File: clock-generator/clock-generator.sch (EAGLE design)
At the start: 106 parts, among them IC1 TLV9001, IC2 24C00TS, K1 694108106102, M1 MENTOR_12701001, T1 BC847, U1 SN74LVC1G04DBV, U2 SI5351C, U3 IP4234CZ6, U4 ATSAMD21E, U5 ADP151AUJZ, U6 IP4234CZ6, X1 MINI-USB-SHIELD-UX60A-MB-5ST, X4 JACK2.5_SJ-2523, X5 UEXT/90

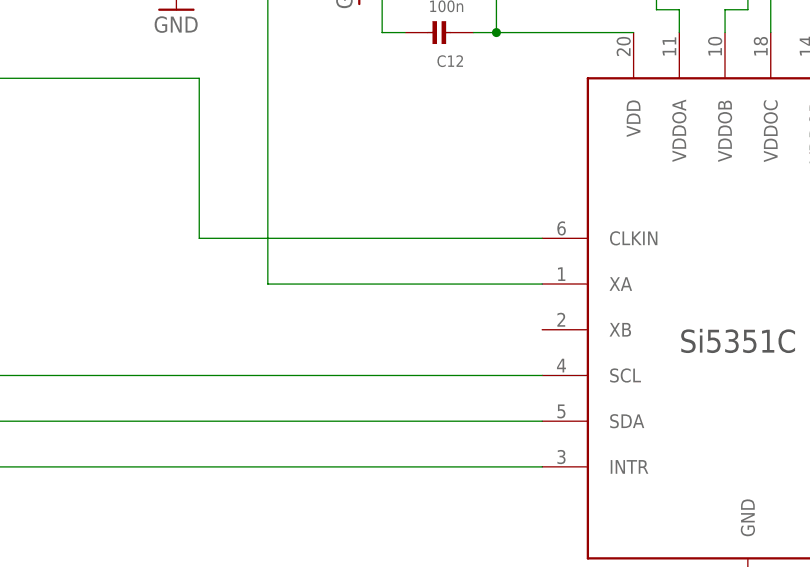
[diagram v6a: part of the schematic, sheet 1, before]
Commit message: osmo-clock-gen: capacitive coupling for XA input needed - added 100n
This was a remark by tnt, thanks.
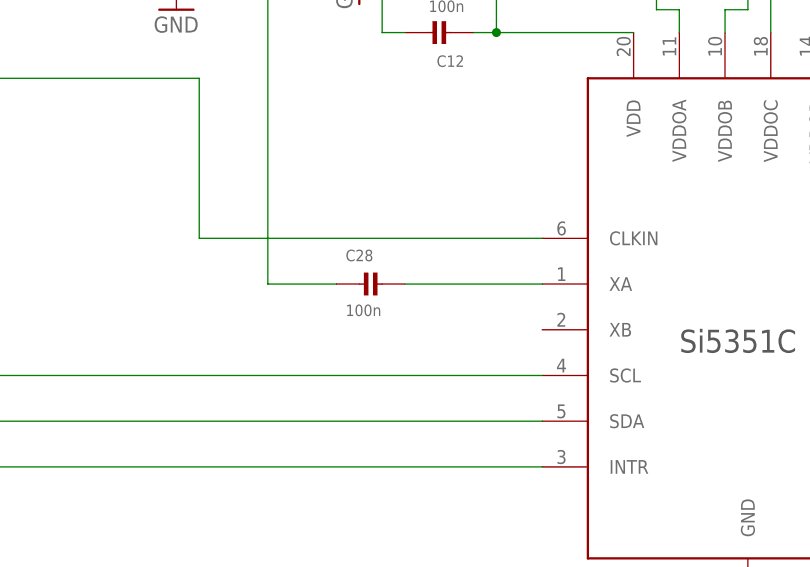
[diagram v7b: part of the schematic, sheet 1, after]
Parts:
- added C28: 100n, rc-sysmocom:CAP_CERAMIC_0603
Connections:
- new net N$8: C28.2, U2.XA
- net N$4: now also C28.1; no longer U2.XA

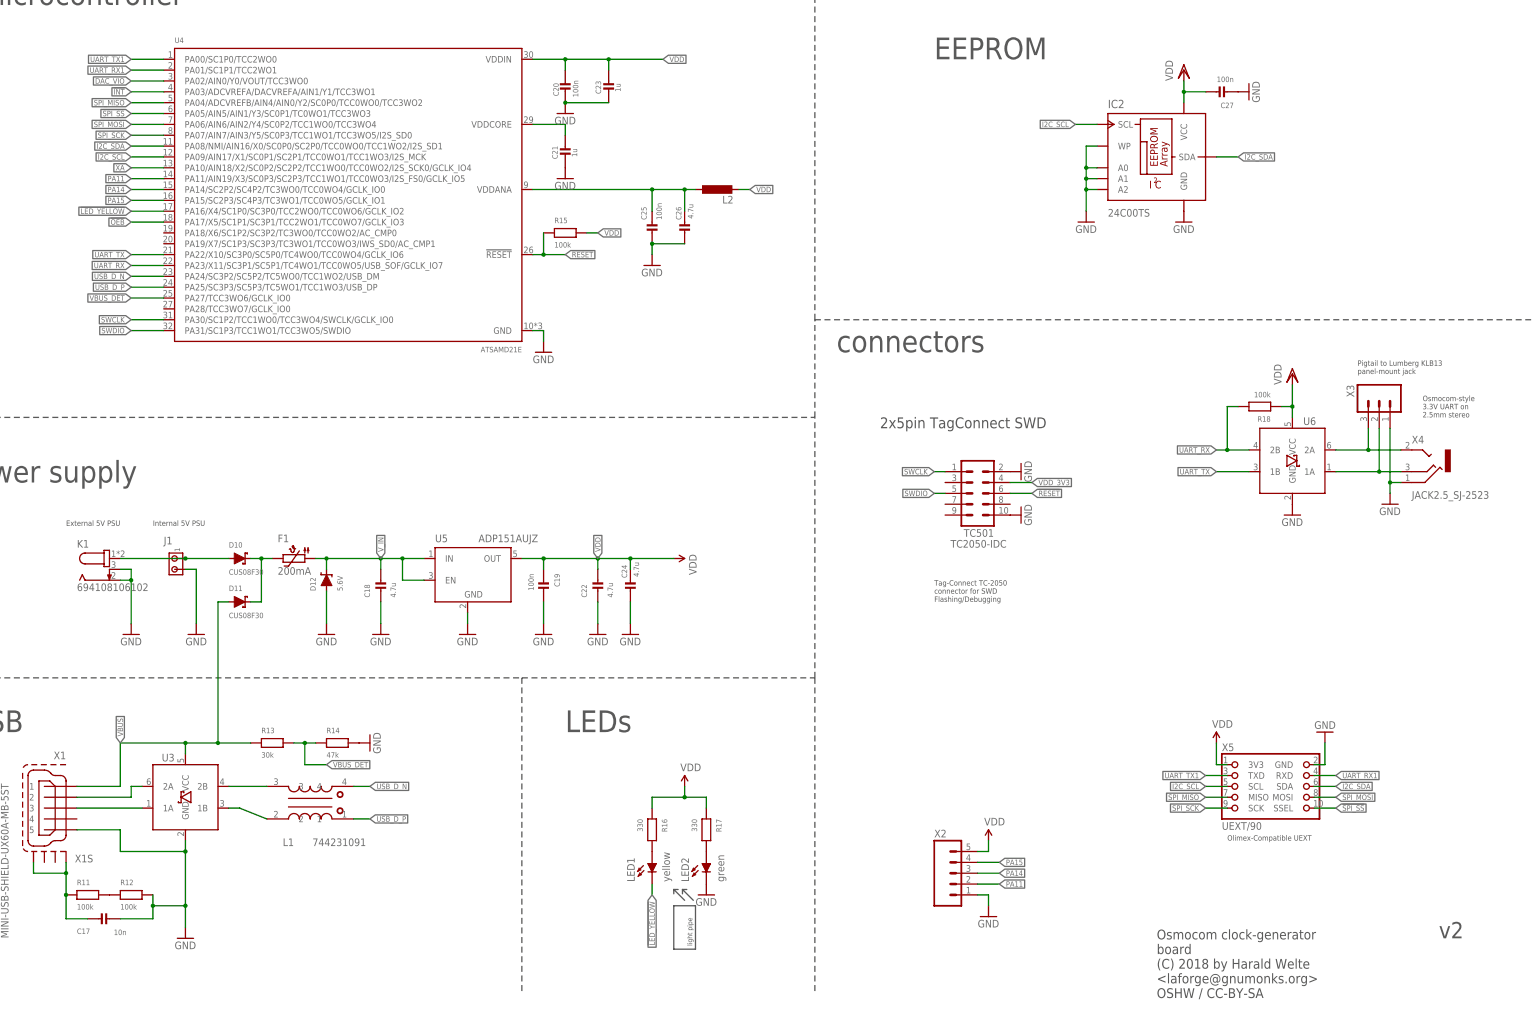
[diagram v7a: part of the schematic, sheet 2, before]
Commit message: <osmo-clock-gen: add more TVS for exposed signals, clean up and finish
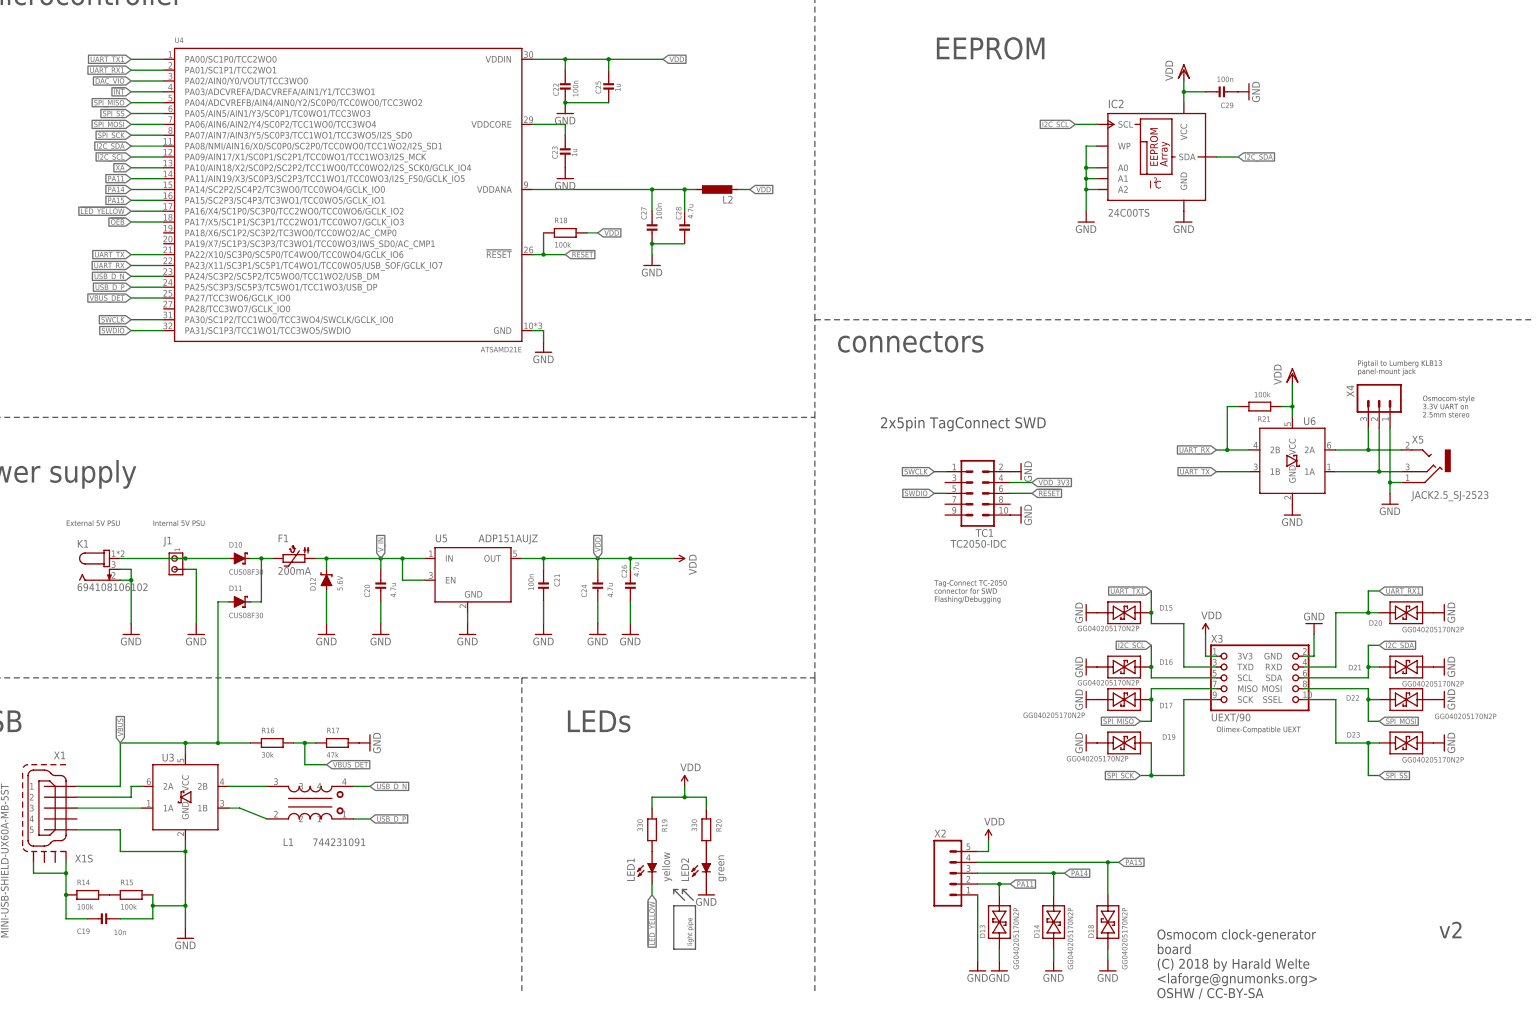
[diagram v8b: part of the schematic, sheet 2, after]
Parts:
- added C29: 100n, rc-sysmocom:CAP_CERAMIC_0603
- added D13, D14, D15, D16, D17, D18, D19, D20, D21, D22, D23: GG040205170N2P, diodes-sysmocom:TVSDIODE-BIDI-0402
- C1, C19, C2: value 100n -> 10n; device rc-sysmocom:CAP_CERAMIC_0603 -> rc-sysmocom:CAP_CERAMIC_0402; DESCRIPTION CAP CER 0.1UF 16V X7R 0603 -> CAP CER 10000PF 25V X7R 0402; LINK https://www.digikey.de/product-detail/de/samsung-electro-mechanics/CL10B104KO8NNNC/1276-1005-1-ND/3889091 -> https://www.digikey.de/product-detail/de/samsung-electro-mechanics/CL05B103KA5NNNC/1276-1057-1-ND/3889143; MANUFACTURERPARTNUMBER CL10B104KO8NNNC -> CL05B103KA5NNNC; SOURCEPARTNUMBER 1276-1005-1-ND -> 1276-1057-1-ND
- C10: value 22u -> 100n; device rc-sysmocom:CAP_CERAMIC_0805 -> rc-sysmocom:CAP_CERAMIC_0402; DESCRIPTION CAP CER 22UF 6.3V 20% X5R 0805 -> NO DESCRIPTION; LINK http://www.digikey.de/product-detail/de/CL21A226MQQNNNE/127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 -> UNKNOWN LINK; MANUFACTURER Samsung Electro-Mechanics America, Inc -> UNKNOWN MANUFACTURER; MANUFACTURERPARTNUMBER CL21A226MQQNNNE -> UNKNOWN MANUFACTURER PART NUMBER; POPULATED FALSE -> TRUE; ROHSCERTIFICATE Bleifrei / RoHS-konform -> UNKNOWN ROHS CERTIFICATE; SOURCE DIGIKEY -> UNKNOWN SOURCE; SOURCEPARTNUMBER 1276-1100-1-ND -> UNKNOWN SOURCE PART NUMBER
- C11, C21: value 1u -> 100n; DESCRIPTION CAP CER 1UF 10V X5R 0603 -> CAP CER 0.1UF 16V X7R 0603; LINK https://www.digikey.de/product-detail/de/samsung-electro-mechanics/CL10A105KP8NNNC/1276-1182-1-ND/3889268 -> https://www.digikey.de/product-detail/de/samsung-electro-mechanics/CL10B104KO8NNNC/1276-1005-1-ND/3889091; MANUFACTURERPARTNUMBER CL10A105KP8NNNC -> CL10B104KO8NNNC; SOURCEPARTNUMBER 1276-1182-1-ND -> 1276-1005-1-ND
- C12: value 100n -> 22u; device rc-sysmocom:CAP_CERAMIC_0603 -> rc-sysmocom:CAP_CERAMIC_0805; DESCRIPTION CAP CER 0.1UF 16V X7R 0603 -> CAP CER 22UF 6.3V 20% X5R 0805; LINK https://www.digikey.de/product-detail/de/samsung-electro-me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 -> http://www.digikey.de/product-detail/de/CL21A226MQQNNNE/127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; MANUFACTURER Samsung Electro-Mechanics -> Samsung Electro-Mechanics America, Inc; MANUFACTURERPARTNUMBER CL10B104KO8NNNC -> CL21A226MQQNNNE; POPULATED TRUE -> FALSE; SOURCEPARTNUMBER 1276-1005-1-ND -> 1276-1100-1-ND
- C13, C9: value 100n -> 1u; device rc-sysmocom:CAP_CERAMIC_0402 -> rc-sysmocom:CAP_CERAMIC_0603; DESCRIPTION NO DESCRIPTION -> CAP CER 1UF 10V X5R 0603; LINK UNKNOWN LINK -> https://www.digikey.de/product-detail/de/samsung-electro-me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; MANUFACTURER UNKNOWN MANUFACTURER -> Samsung Electro-Mechanics; MANUFACTURERPARTNUMBER UNKNOWN MANUFACTURER PART NUMBER -> CL10A105KP8NNNC; ROHSCERTIFICATE UNKNOWN ROHS CERTIFICATE -> Bleifrei / RoHS-konform; SOURCE UNKNOWN SOURCE -> DIGIKEY; SOURCEPARTNUMBER UNKNOWN SOURCE PART NUMBER -> 1276-1182-1-ND
- C14: device rc-sysmocom:CAP_CERAMIC_0402 -> rc-sysmocom:CAP_CERAMIC_0603; DESCRIPTION NO DESCRIPTION -> CAP CER 0.1UF 16V X7R 0603; LINK UNKNOWN LINK -> https://www.digikey.de/product-detail/de/samsung-electro-me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; MANUFACTURER UNKNOWN MANUFACTURER -> Samsung Electro-Mechanics; MANUFACTURERPARTNUMBER UNKNOWN MANUFACTURER PART NUMBER -> CL10B104KO8NNNC; ROHSCERTIFICATE UNKNOWN ROHS CERTIFICATE -> Bleifrei / RoHS-konform; SOURCE UNKNOWN SOURCE -> DIGIKEY; SOURCEPARTNUMBER UNKNOWN SOURCE PART NUMBER -> 1276-1005-1-ND
- C17: value 10n -> 100n; DESCRIPTION CAP CER 10000PF 25V X7R 0402 -> NO DESCRIPTION; LINK https://www.digikey.de/product-detail/de/samsung-electro-me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 -> UNKNOWN LINK; MANUFACTURER Samsung Electro-Mechanics -> UNKNOWN MANUFACTURER; MANUFACTURERPARTNUMBER CL05B103KA5NNNC -> UNKNOWN MANUFACTURER PART NUMBER; ROHSCERTIFICATE Bleifrei / RoHS-konform -> UNKNOWN ROHS CERTIFICATE; SOURCE DIGIKEY -> UNKNOWN SOURCE; SOURCEPARTNUMBER 1276-1057-1-ND -> UNKNOWN SOURCE PART NUMBER
- C18: value 4.7u -> 100n; device rc-sysmocom:CAP_CERAMIC_0805 -> rc-sysmocom:CAP_CERAMIC_0402; DESCRIPTION CAP CER 4.7UF 16V X5R 0805 -> NO DESCRIPTION; LINK https://www.digikey.de/product-detail/de/samsung-electro-me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 -> UNKNOWN LINK; MANUFACTURER Samsung Electro-Mechanics -> UNKNOWN MANUFACTURER; MANUFACTURERPARTNUMBER CL21A475KOFNNNE -> UNKNOWN MANUFACTURER PART NUMBER; ROHSCERTIFICATE Bleifrei / RoHS-konform -> UNKNOWN ROHS CERTIFICATE; SOURCE DIGIKEY -> UNKNOWN SOURCE; SOURCEPARTNUMBER 1276-1065-1-ND -> UNKNOWN SOURCE PART NUMBER
- C20: value 100n -> 4.7u; device rc-sysmocom:CAP_CERAMIC_0402 -> rc-sysmocom:CAP_CERAMIC_0805; DESCRIPTION CAP CER 0.1UF 10V X5R 0402 -> CAP CER 4.7UF 16V X5R 0805; LINK https://www.digikey.de/product-detail/de/samsung-electro-mechanics/CL05A104MP5NNNC/1276-1443-1-ND/3889529 -> https://www.digikey.de/product-detail/de/samsung-electro-mechanics/CL21A475KOFNNNE/1276-1065-1-ND/3889151; MANUFACTURERPARTNUMBER CL05A104MP5NNNC -> CL21A475KOFNNNE; SOURCEPARTNUMBER 1276-1443-1-ND -> 1276-1065-1-ND
- C22: value 4.7u -> 100n; device rc-sysmocom:CAP_CERAMIC_0805 -> rc-sysmocom:CAP_CERAMIC_0402; DESCRIPTION CAP CER 4.7UF 16V X5R 0805 -> CAP CER 0.1UF 10V X5R 0402; LINK https://www.digikey.de/product-detail/de/samsung-electro-mechanics/CL21A475KOFNNNE/1276-1065-1-ND/3889151 -> https://www.digikey.de/product-detail/de/samsung-electro-mechanics/CL05A104MP5NNNC/1276-1443-1-ND/3889529; MANUFACTURERPARTNUMBER CL21A475KOFNNNE -> CL05A104MP5NNNC; SOURCEPARTNUMBER 1276-1065-1-ND -> 1276-1443-1-ND
- C25: value 100n -> 1u; device rc-sysmocom:CAP_CERAMIC_0402 -> rc-sysmocom:CAP_CERAMIC_0603; DESCRIPTION CAP CER 0.1UF 10V X5R 0402 -> CAP CER 1UF 10V X5R 0603; LINK https://www.digikey.de/product-detail/de/samsung-electro-mechanics/CL05A104MP5NNNC/1276-1443-1-ND/3889529 -> https://www.digikey.de/product-detail/de/samsung-electro-mechanics/CL10A105KP8NNNC/1276-1182-1-ND/3889268; MANUFACTURERPARTNUMBER CL05A104MP5NNNC -> CL10A105KP8NNNC; SOURCEPARTNUMBER 1276-1443-1-ND -> 1276-1182-1-ND
- C27: device rc-sysmocom:CAP_CERAMIC_0603 -> rc-sysmocom:CAP_CERAMIC_0402; DESCRIPTION CAP CER 0.1UF 16V X7R 0603 -> CAP CER 0.1UF 10V X5R 0402; LINK https://www.digikey.de/product-detail/de/samsung-electro-mechanics/CL10B104KO8NNNC/1276-1005-1-ND/3889091 -> https://www.digikey.de/product-detail/de/samsung-electro-mechanics/CL05A104MP5NNNC/1276-1443-1-ND/3889529; MANUFACTURERPARTNUMBER CL10B104KO8NNNC -> CL05A104MP5NNNC; SOURCEPARTNUMBER 1276-1005-1-ND -> 1276-1443-1-ND
- C28: value 100n -> 4.7u; device rc-sysmocom:CAP_CERAMIC_0603 -> rc-sysmocom:CAP_CERAMIC_0805; DESCRIPTION CAP CER 0.1UF 16V X7R 0603 -> CAP CER 4.7UF 16V X5R 0805; LINK https://www.digikey.de/product-detail/de/samsung-electro-mechanics/CL10B104KO8NNNC/1276-1005-1-ND/3889091 -> https://www.digikey.de/product-detail/de/samsung-electro-mechanics/CL21A475KOFNNNE/1276-1065-1-ND/3889151; MANUFACTURERPARTNUMBER CL10B104KO8NNNC -> CL21A475KOFNNNE; SOURCEPARTNUMBER 1276-1005-1-ND -> 1276-1065-1-ND
- C3, C4: value 10n -> 100n; device rc-sysmocom:CAP_CERAMIC_0402 -> rc-sysmocom:CAP_CERAMIC_0603; DESCRIPTION CAP CER 10000PF 25V X7R 0402 -> CAP CER 0.1UF 16V X7R 0603; LINK https://www.digikey.de/product-detail/de/samsung-electro-mechanics/CL05B103KA5NNNC/1276-1057-1-ND/3889143 -> https://www.digikey.de/product-detail/de/samsung-electro-mechanics/CL10B104KO8NNNC/1276-1005-1-ND/3889091; MANUFACTURERPARTNUMBER CL05B103KA5NNNC -> CL10B104KO8NNNC; SOURCEPARTNUMBER 1276-1057-1-ND -> 1276-1005-1-ND
- J1: CLASS (none) -> CONNECTOR\JUMPER; DESCRIPTION (none) -> NO DESCRIPTION; LINK (none) -> UNKNOWN LINK; MANUFACTURER (none) -> UNKNOWN MANUFACTURER; MANUFACTURERPARTNUMBER (none) -> UNKNOWN MANUFACTURER PART NUMBER; POPULATED (none) -> TRUE; ROHSCERTIFICATE (none) -> UNKNOWN ROHS CERTIFICATE; SOURCE (none) -> UNKNOWN SOURCE; SOURCEPARTNUMBER (none) -> UNKNOWN SOURCE PART NUMBER
- R11: value 100k -> 0; DESCRIPTION RES SMD 100K OHM 5%% 1/10W 0603 -> RES 0.0 OHM 1/10W JUMP 0603; LINK https://www.digikey.de/product-detail/de/yageo/RC0603JR-071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 -> http://www.digikey.de/product-detail/de/foo/1276-3510-1-ND; MANUFACTURER Yageo -> Samsung Electro-Mechanics America, Inc; MANUFACTURERPARTNUMBER RC0603JR-07100KL -> RC1608J000CS; SOURCEPARTNUMBER 311-100KGRCT-ND -> 1276-3510-1-ND
- R12: value 100k -> 47k; DESCRIPTION RES SMD 100K OHM 5%% 1/10W 0603 -> RES SMD 47K OHM 5%% 1/10W 0603; LINK https://www.digikey.de/product-detail/de/yageo/RC0603JR-071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 -> https://www.digikey.de/product-detail/de/yageo/RC0603JR-074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; MANUFACTURERPARTNUMBER RC0603JR-07100KL -> RC0603JR-0747KL; SOURCEPARTNUMBER 311-100KGRCT-ND -> 311-47KGRCT-ND
- R14: value 47k -> 100k; DESCRIPTION RES SMD 47K OHM 5%% 1/10W 0603 -> RES SMD 100K OHM 5%% 1/10W 0603; LINK https://www.digikey.de/product-detail/de/yageo/RC0603JR-074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 -> https://www.digikey.de/product-detail/de/yageo/RC0603JR-071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; MANUFACTURERPARTNUMBER RC0603JR-0747KL -> RC0603JR-07100KL; SOURCEPARTNUMBER 311-47KGRCT-ND -> 311-100KGRCT-ND
- R16: value 330 -> 30k; DESCRIPTION RES 330 OHM 5%% 1/10W 0603 -> RES SMD 30K OHM 5%% 1/10W 0603; LINK https://www.digikey.de/product-detail/de/stackpole-electron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 -> https://www.digikey.de/product-detail/de/yageo/RC0603JR-073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; MANUFACTURER Stackpole Electronics Inc. -> Yageo; MANUFACTURERPARTNUMBER RMCF0603JT330R -> RC0603JR-0730KL; SOURCEPARTNUMBER RMCF0603JT330RCT-ND -> 311-30KGRCT-ND
- R17: value 330 -> 47k; DESCRIPTION RES 330 OHM 5%% 1/10W 0603 -> RES SMD 47K OHM 5%% 1/10W 0603; LINK https://www.digikey.de/product-detail/de/stackpole-electron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 -> https://www.digikey.de/product-detail/de/yageo/RC0603JR-074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; MANUFACTURER Stackpole Electronics Inc. -> Yageo; MANUFACTURERPARTNUMBER RMCF0603JT330R -> RC0603JR-0747KL; SOURCEPARTNUMBER RMCF0603JT330RCT-ND -> 311-47KGRCT-ND
- R19: value 30k -> 330; DESCRIPTION RES SMD 30K OHM 5%% 1/10W 0603 -> RES 330 OHM 5%% 1/10W 0603; LINK https://www.digikey.de/product-detail/de/yageo/RC0603JR-073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 -> https://www.digikey.de/product-detail/de/stackpole-electron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; MANUFACTURER Yageo -> Stackpole Electronics Inc.; MANUFACTURERPARTNUMBER RC0603JR-0730KL -> RMCF0603JT330R; SOURCEPARTNUMBER 311-30KGRCT-ND -> RMCF0603JT330RCT-ND
- R20: value 47k -> 330; DESCRIPTION RES SMD 47K OHM 5%% 1/10W 0603 -> RES 330 OHM 5%% 1/10W 0603; LINK https://www.digikey.de/product-detail/de/yageo/RC0603JR-074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 -> https://www.digikey.de/product-detail/de/stackpole-electron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; MANUFACTURER Yageo -> Stackpole Electronics Inc.; MANUFACTURERPARTNUMBER RC0603JR-0747KL -> RMCF0603JT330R; SOURCEPARTNUMBER 311-47KGRCT-ND -> RMCF0603JT330RCT-ND
- R21: value 0 -> 100k; DESCRIPTION RES 0.0 OHM 1/10W JUMP 0603 -> RES SMD 100K OHM 5%% 1/10W 0603; LINK http://www.digikey.de/product-detail/de/foo/1276-3510-1-ND -> https://www.digikey.de/product-detail/de/yageo/RC0603JR-071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; MANUFACTURER Samsung Electro-Mechanics America, Inc -> Yageo; MANUFACTURERPARTNUMBER RC1608J000CS -> RC0603JR-07100KL; SOURCEPARTNUMBER 1276-3510-1-ND -> 311-100KGRCT-ND
- X3: value (none) -> UEXT/90; device laforge:PINHD-1X3LOCK_NO_SILK -> laforge:UEXT/90; DESCRIPTION NO DESCRIPTION -> CONN HEADER VERT 10POS 2.54MM; LINK UNKNOWN LINK -> https://www.digikey.de/product-detail/de/on-shore-technolog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; MANUFACTURER UNKNOWN MANUFACTURER -> On Shore Technology Inc.; MANUFACTURERPARTNUMBER UNKNOWN MANUFACTURER PART NUMBER -> 302-S101; POPULATED FALSE -> TRUE; ROHSCERTIFICATE UNKNOWN ROHS CERTIFICATE -> Bleifrei / RoHS-konform; SOURCE UNKNOWN SOURCE -> DIGIKEY; SOURCEPARTNUMBER UNKNOWN SOURCE PART NUMBER -> ED1543-ND
- X4: value JACK2.5_SJ-2523 -> (none); device laforge:JACK2.5_SJ-2523 -> laforge:PINHD-1X3LOCK_NO_SILK; DESCRIPTION CONN JACK STEREO 2.5MM SMD R/A -> NO DESCRIPTION; LINK https://www.digikey.de/product-detail/de/cui-inc/SJ-2523-SM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 -> UNKNOWN LINK; MANUFACTURER CUI Inc. -> UNKNOWN MANUFACTURER; MANUFACTURERPARTNUMBER SJ-2523-SMT-TR -> UNKNOWN MANUFACTURER PART NUMBER; POPULATED TRUE -> FALSE; ROHSCERTIFICATE Bleifrei / RoHS-konform -> UNKNOWN ROHS CERTIFICATE; SOURCE DIGIKEY -> UNKNOWN SOURCE; SOURCEPARTNUMBER CP-2523SJCT-ND -> UNKNOWN SOURCE PART NUMBER
- X5: value UEXT/90 -> JACK2.5_SJ-2523; device laforge:UEXT/90 -> laforge:JACK2.5_SJ-2523; DESCRIPTION CONN HEADER VERT 10POS 2.54MM -> CONN JACK STEREO 2.5MM SMD R/A; LINK https://www.digikey.de/product-detail/de/on-shore-technolog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 -> https://www.digikey.de/product-detail/de/cui-inc/SJ-2523-SM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; MANUFACTURER On Shore Technology Inc. -> CUI Inc.; MANUFACTURERPARTNUMBER 302-S101 -> SJ-2523-SMT-TR; SOURCEPARTNUMBER ED1543-ND -> CP-2523SJCT-ND
- renumbered TC501 to TC1
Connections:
- net !RESET: now also R18.2; no longer R15.2
- net !SPI_SS: now also D23.P$2, X3.SSEL; no longer X5.SSEL
- net CLKIN: now also C4.1; no longer C2.1
- net CLKIN_AC: now also C4.2; no longer C2.2
- net GND: now also C12.1, C13.1, C18.2, C2.1, C21.2, C28.1, C29.1, C9.2, D13.P$1, D14.P$1, D15.P$2, D16.P$2, D17.P$2, D18.P$1, D19.P$1, D20.P$1, D21.P$1, D22.P$1, D23.P$1, R13.2, R15.1, R17.1, X3.GND, X4.1, X5.RING; no longer C11.1, C12.2, C13.2, C18.1, C21.1, C4.1, C9.1, R12.1, R14.1, R19.2, X3.1, X4.RING, X5.GND
- net I2C_SCL: now also D16.P$1, X3.SCL; no longer X5.SCL
- net I2C_SDA: now also D21.P$2, X3.SDA; no longer X5.SDA
- net N$1: now also C23.2; no longer C21.2
- net N$11: now also R20.1; no longer R17.1
- net N$12: now also R19.1; no longer R16.1
- net N$13: now also C27.2, C28.2; no longer C25.2, C26.2
- net N$2: now also R11.1, R12.1; no longer R20.1, R21.1
- net N$4: now also C11.1, R12.2, R13.1; no longer C28.1, R19.1, R20.2
- net N$55: now also R14.1, R15.2; no longer R11.1, R12.2
- net N$61: now also C19.1, R14.2; no longer C17.1, R11.2
- net N$8: now also C11.2; no longer C28.2
- net PA11: now also D13.P$2
- net PA14: now also D14.P$2
- net PA15: now also D18.P$2
- net SPI_MISO: now also D17.P$1, X3.MISO; no longer X5.MISO
- net SPI_MOSI: now also D22.P$2, X3.MOSI; no longer X5.MOSI
- net SPI_SCK: now also D19.P$2, X3.SCK; no longer X5.SCK
- net UART_RX: now also R21.1; no longer R18.1
- net UART_RX0: now also X4.3, X5.TIP; no longer X3.3, X4.TIP
- net UART_RX1: now also D20.P$2, X3.RXD; no longer X5.RXD
- net UART_TX0: now also X4.2, X5.MIDDLE; no longer X3.2, X4.MIDDLE
- net UART_TX1: now also D15.P$1, X3.TXD; no longer X5.TXD
- net VBUS: now also R16.2; no longer R13.2
- net VBUS_DET: now also R16.1, R17.2; no longer R13.1, R14.2
- net VDD: now also C13.2, C14.1, C2.2, C21.1, C25.2, C26.2, C29.2, R18.1, R19.2, R20.2, R21.2, X3.3V3; no longer C11.2, C12.1, C19.1, C20.2, C23.2, C27.2, C4.2, R15.1, R16.2, R17.2, R18.2, X5.3V3
- net VDDIO_ADJ: now also C12.2; no longer C9.2
- net VDDOA: now also C18.1; no longer C16.1
- net VDDOB: now also C17.1; no longer C15.1
- net VDDOC: now also C16.1; no longer C14.1
- net VDDOD: now also C15.1; no longer C13.1
- net V_IN: now also C20.2, C9.1; no longer C18.2
- net XA: now also R11.2; no longer R21.2
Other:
- moved on the sheet: C1, C10, C11, C12, C13, C14, C15, C16, C19, C2, C20, C21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
